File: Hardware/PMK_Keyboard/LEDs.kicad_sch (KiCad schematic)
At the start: 40 parts

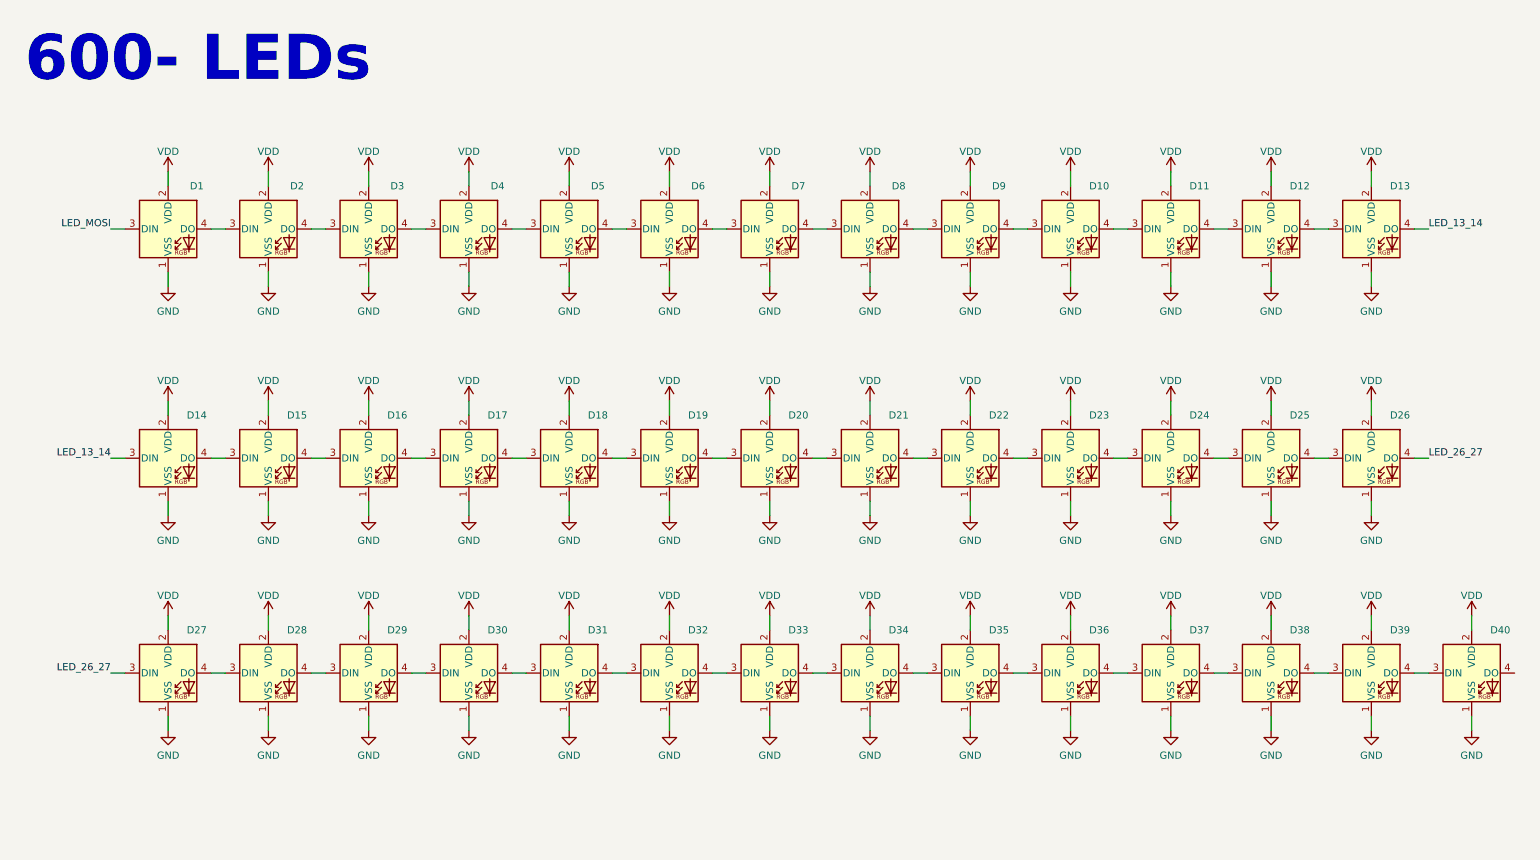
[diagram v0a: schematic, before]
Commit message: Worked on hierachic page again
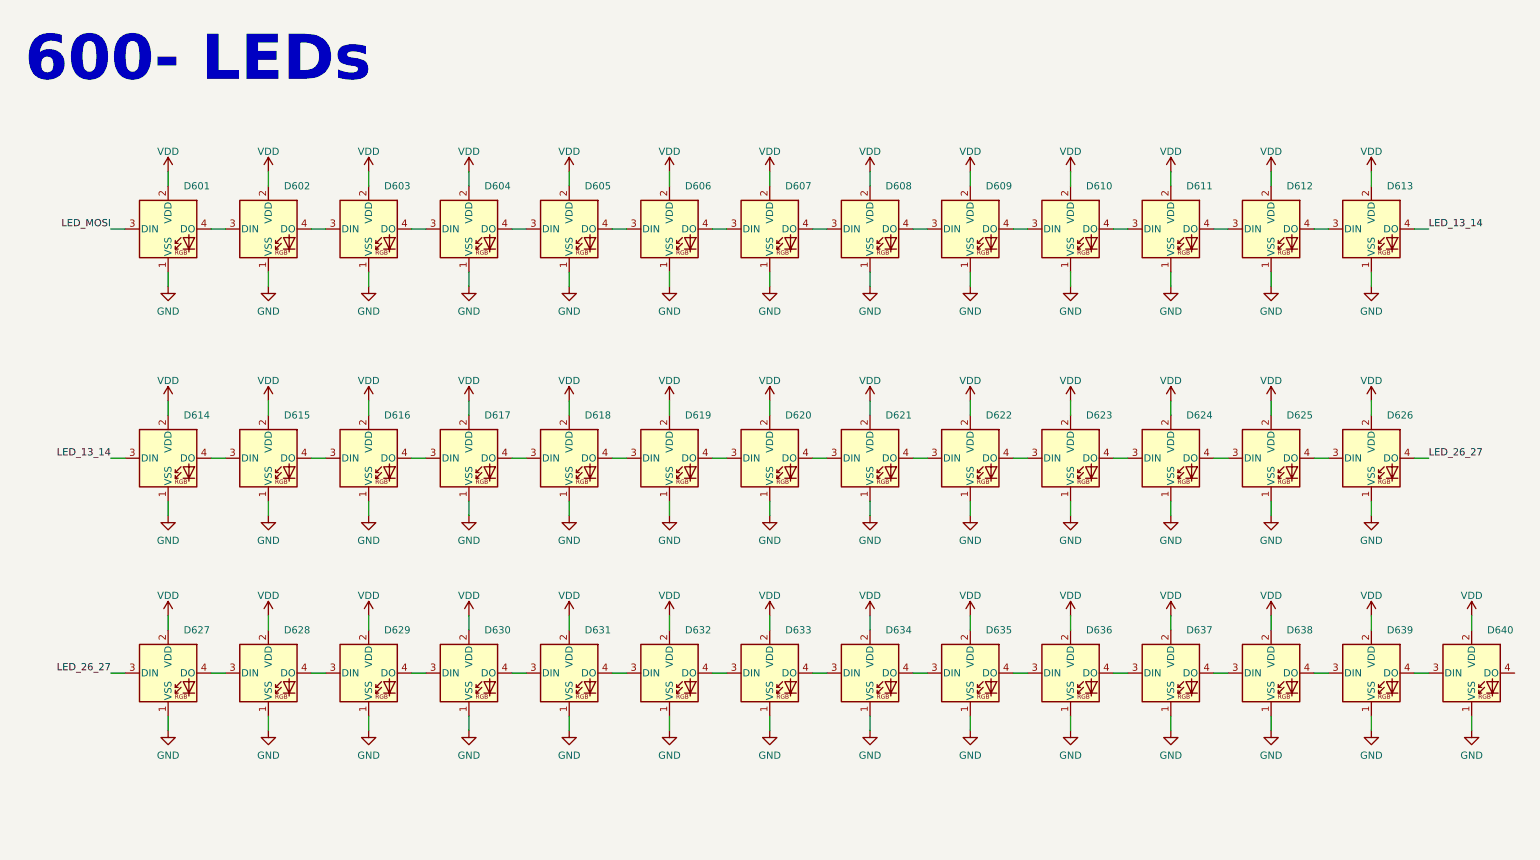
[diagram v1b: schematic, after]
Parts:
- renumbered D1 to D601, D2 to D602, D3 to D603, D4 to D604, D5 to D605, D6 to D606, D7 to D607, D8 to D608, D9 to D609, D10 to D610, D11 to D611, D12 to D612, D13 to D613, D14 to D614, D15 to D615, D16 to D616, D17 to D617, D18 to D618, D19 to D619, D20 to D620, D21 to D621, D22 to D622, D23 to D623, D24 to D624, D25 to D625, D26 to D626, D27 to D627, D28 to D628, D29 to D629, D30 to D630, D31 to D631, D32 to D632, D33 to D633, D34 to D634, D35 to D635, D36 to D636, D37 to D637, D38 to D638, D39 to D639, D40 to D640

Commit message: Again on hierachic sheet
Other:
- company: (none) -> PumaCorp
- title: (none) -> PMK_Keyboard
- moved on the sheet: D601, D602, D603, D604, D605, D606, D607, D608, D609, D610, D611, D612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

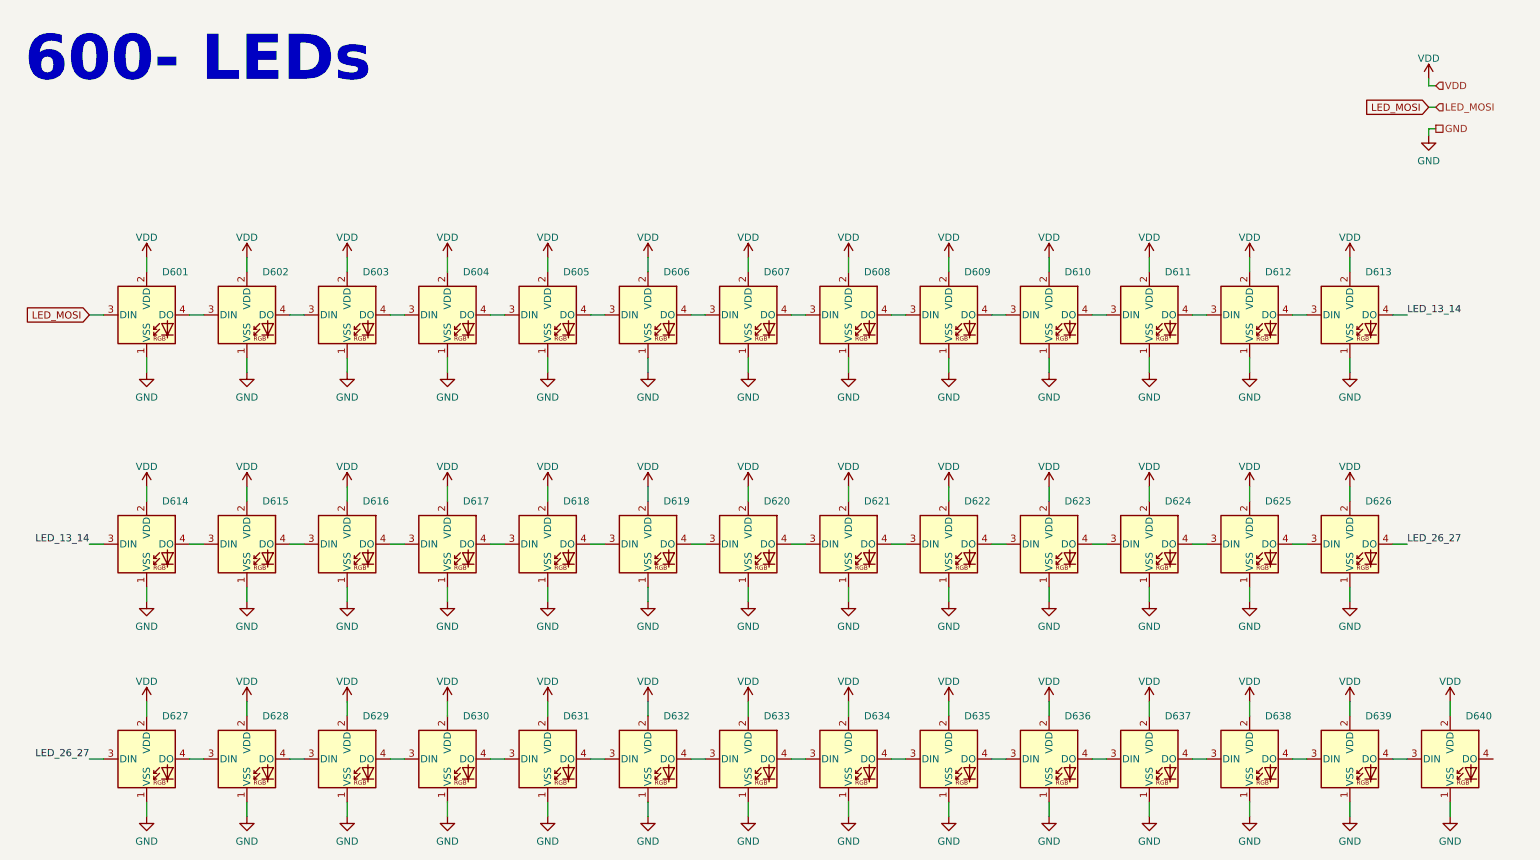
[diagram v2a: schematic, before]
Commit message: Schematic is done, only possible update is change of ESP pins
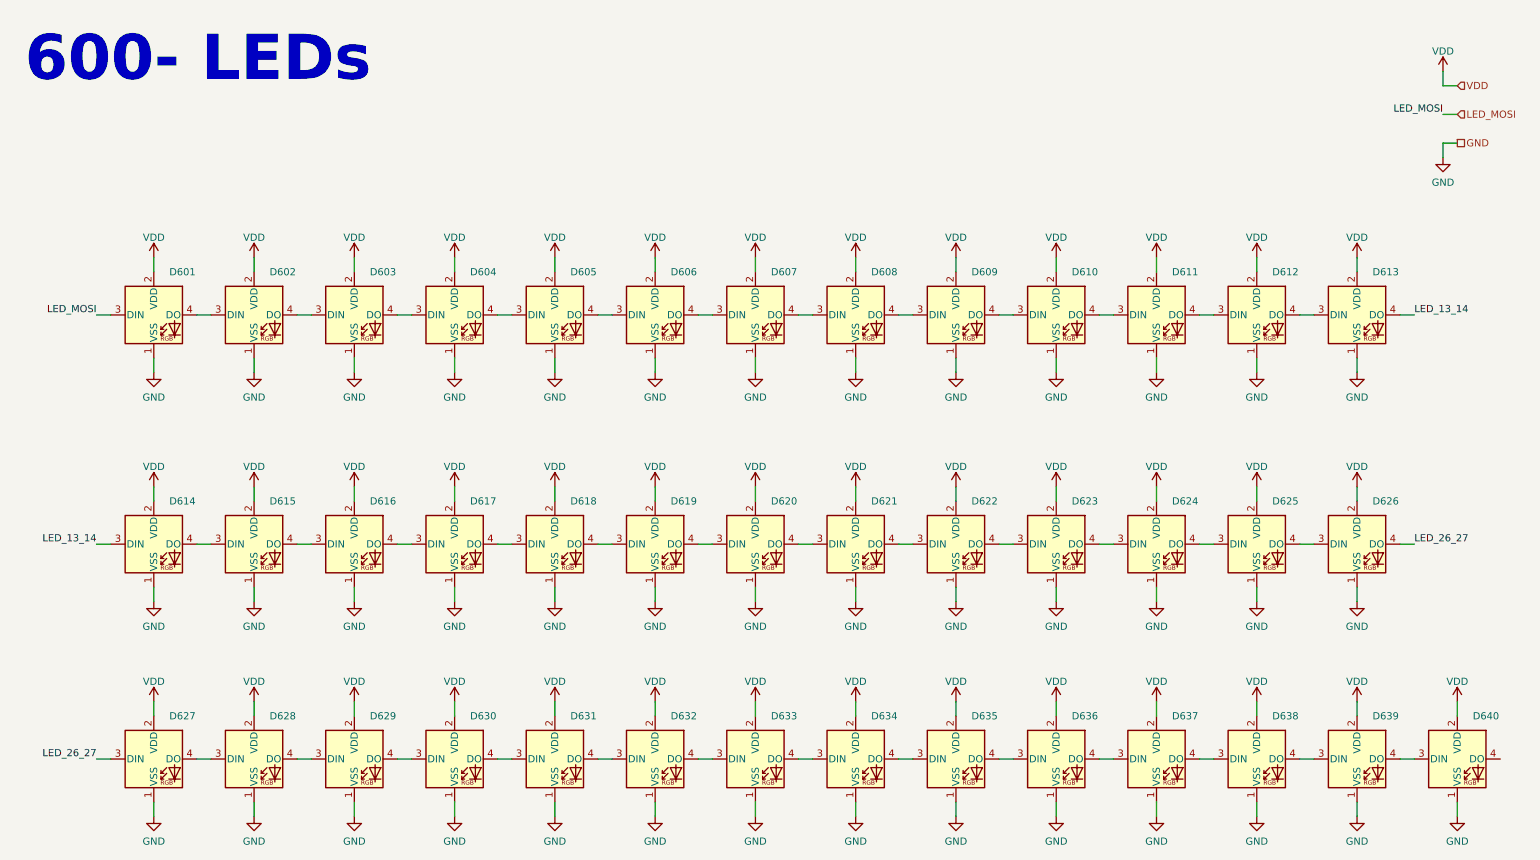
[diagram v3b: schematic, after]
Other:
- moved on the sheet: D601, D602, D603, D604, D605, D606, D607, D608, D609, D610, D611, D612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
